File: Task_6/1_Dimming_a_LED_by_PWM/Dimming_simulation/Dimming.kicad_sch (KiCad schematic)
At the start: 6 parts, among them Q1 BC817

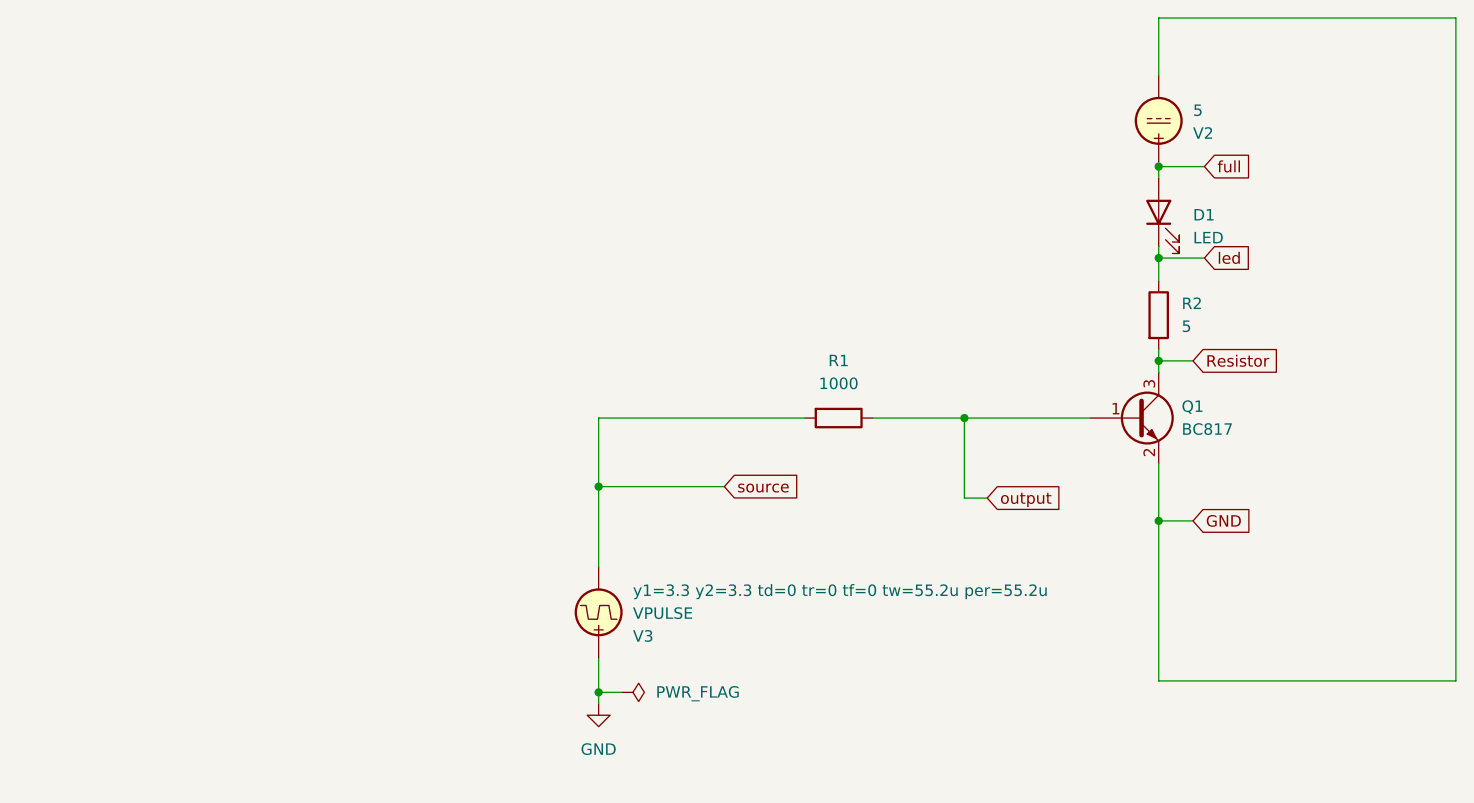
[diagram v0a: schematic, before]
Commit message: add simulation and measurement of current through LED
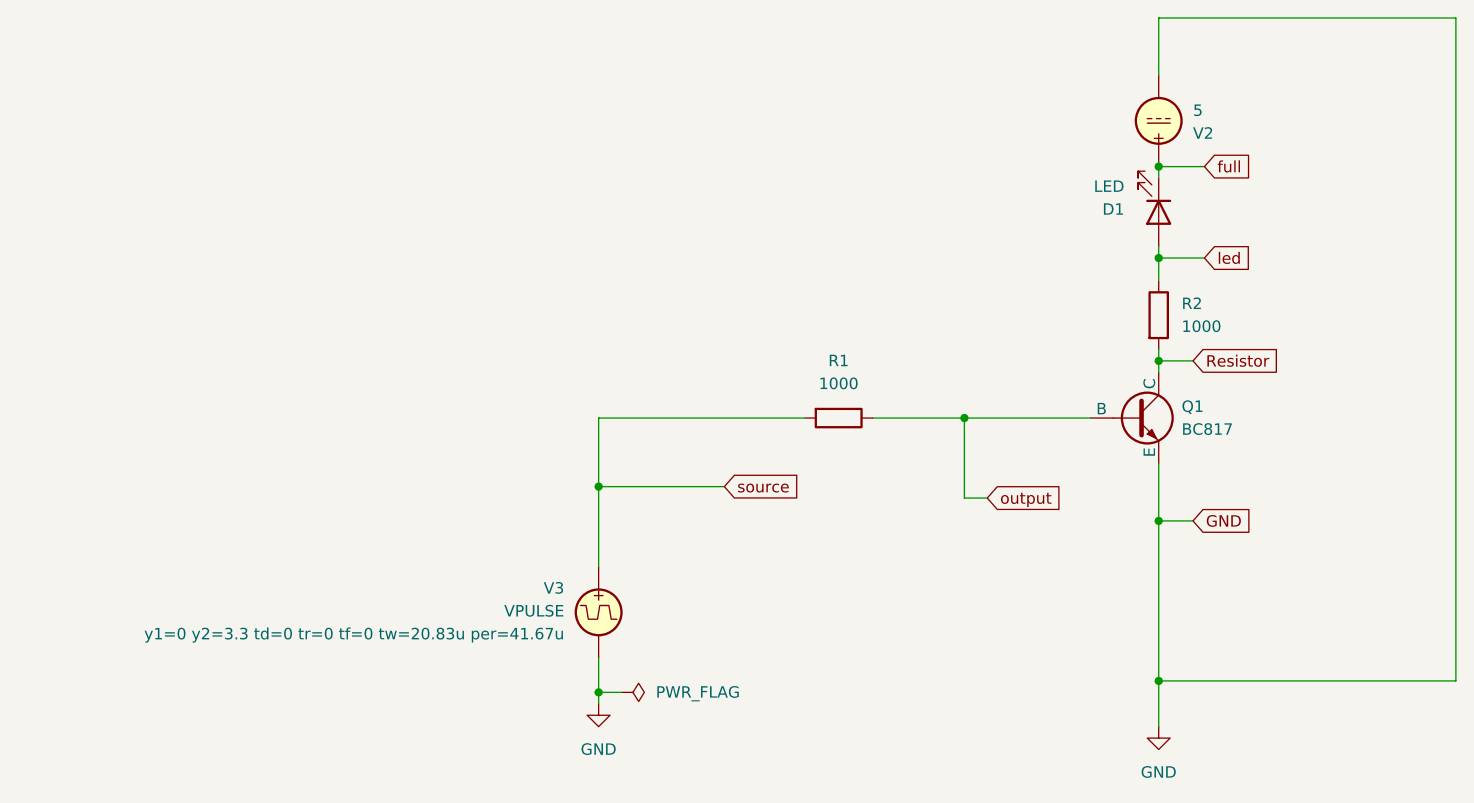
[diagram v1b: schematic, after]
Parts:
- removed Q1: BC817, Package_TO_SOT_SMD:SOT-23, symbol Transistor_BJT:BC817
- added Q1: BC817, symbol Simulation_SPICE:NPN
- R2: value 5 -> 1000
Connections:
- net GND: now also V3.2, Q1.3 (E); no longer V3.1
- net Resistor: now also Q1.1 (C)
- net full: now also D1.1 (K); no longer D1.2 (A)
- net led: now also D1.2 (A); no longer D1.1 (K)
- net output: now also Q1.2 (B)
- net source: now also V3.1; no longer V3.2
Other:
- moved on the sheet: D1
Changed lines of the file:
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@@
+	)
+	(junction
+		(at 146.05 113.03)
+		(diameter 0)
+		(color 0 0 0 0)
 	)
 	(junction
@@
 		(pts
 			(xy 149.86 77.47) (xy 146.05 77.47)
+		)
+		(stroke
+			(width 0)
+			(type default)
+		)
+	)
+	(wire
+		(pts
+			(xy 146.05 113.03) (xy 146.05 118.11)
 		)
 		(stroke
@@
 	(symbol
 		(lib_id "Device:LED")
-		(at 146.05 60.96 90)
+		(at 146.05 60.96 270)
 		(unit 1)
 		(exclude_from_sim no)
@@
 		(dnp no)
 		(property "Reference" "D1"
-			(at 149.86 61.2774 90)
+			(at 142.24 60.6426 90)
 			(effects
 				(font
@@
 		)
 		(property "Value" "LED"
-			(at 149.86 63.8174 90)
+			(at 142.24 58.1026 90)
 			(effects
 				(font
@@
 		(lib_id "Simulation_SPICE:VPULSE")
 		(at 83.82 105.41 0)
-		(mirror x)
+		(mirror y)
 		(unit 1)
 		(exclude_from_sim no)
@@
 		(dnp no)
 		(property "Reference" "V3"
-			(at 87.63 108.0799 0)
+			(at 80.01 102.7401 0)
 			(effects
 				(font
@@
 		)
 		(property "Value" "VPULSE"
-			(at 87.63 105.5399 0)
+			(at 80.01 105.2801 0)
 			(effects
 				(font
@@
 			)
 		)
-		(property "Sim.Params" "y1=3.3 y2=3.3 td=0 tr=0 tf=0 tw=55.2u per=55.2u"
-			(at 87.63 102.9999 0)
+		(property "Sim.Params" "y1=0 y2=3.3 td=0 tr=0 tf=0 tw=20.83u per=41.67u"
+			(at 80.01 107.8201 0)
 			(effects
 				(font
@@
 			)
 		)
-		(property "Value" "5"
+		(property "Value" "1000"
 			(at 148.59 73.6599 0)
 			(effects
@@
 	)
 	(symbol
-		(lib_id "Transistor_BJT:BC817")
+		(lib_id "Simulation_SPICE:NPN")
 		(at 143.51 83.82 0)
 		(unit 1)
@@
 		(on_board yes)
 		(dnp no)
+		(fields_autoplaced yes)
 		(property "Reference" "Q1"
 			(at 148.59 82.5499 0)
@@
 			)
 		)
-		(property "Footprint" "Package_TO_SOT_SMD:SOT-23"
-			(at 148.59 85.725 0)
-			(effects
-				(font
-					(size 1.27 1.27)
-					(italic yes)
-				)
-				(justify left)
-				(hide yes)
-			)
-		)
-		(property "Datasheet" "https://www.onsemi.com/pub/Collateral/BC818-D.pdf"
+		(property "Footprint" ""
+			(at 207.01 83.82 0)
+			(effects
+				(font
+					(size 1.27 1.27)
+				)
+				(hide yes)
+			)
+		)
+		(property "Datasheet" "https://ngspice.sourceforge.io/docs/ngspice-html-manual/manual.xhtml#cha_BJTs"
+			(at 207.01 83.82 0)
+			(effects
+				(font
+					(size 1.27 1.27)
+				)
+				(hide yes)
+			)
+		)
+		(property "Description" "Bipolar transistor symbol for simulation only, substrate tied to the emitter"
 			(at 143.51 83.82 0)
 			(effects
@@
 					(size 1.27 1.27)
 				)
-				(justify left)
-				(hide yes)
-			)
-		)
-		(property "Description" "0.8A Ic, 45V Vce, NPN Transistor, SOT-23"
+				(hide yes)
+			)
+		)
+		(property "Sim.Device" "SUBCKT"
+			(at 143.51 83.82 0)
+			(effects
+				(font
+					(size 1.27 1.27)
+				)
+				(hide yes)
+			)
+		)
+		(property "Sim.Pins" "1=1 2=2 3=3"
 			(at 143.51 83.82 0)
 			(effects
@@
 			)
 		)
-		(property "Sim.Device" "SUBCKT"
-			(at 143.51 83.82 0)
-			(effects
-				(font
-					(size 1.27 1.27)
-				)
-				(hide yes)
-			)
-		)
-		(property "Sim.Pins" "1=1 2=2 3=3"
-			(at 143.51 83.82 0)
-			(effects
-				(font
-					(size 1.27 1.27)
-				)
-				(hide yes)
-			)
+		(pin "2"
+		)
+		(pin "3"
 		)
 		(pin "1"
-		)
-		(pin "3"
-		)
-		(pin "2"
 		)
 		(instances
@@
 					(unit 1)
 				)
+			)
+		)
+	)
+	(symbol
+		(lib_id "power:GND")
+		(at 146.05 118.11 0)
+		(unit 1)
+		(exclude_from_sim no)
+		(in_bom yes)
+		(on_board yes)
+		(dnp no)
+		(fields_autoplaced yes)
+		(property "Reference" "#PWR02"
+			(at 146.05 124.46 0)
+			(effects
+				(font
+					(size 1.27 1.27)
+				)
+				(hide yes)
+			)
+		)
+		(property "Value" "GND"
+			(at 146.05 123.19 0)
+			(effects
+				(font
+					(size 1.27 1.27)
+				)
+			)
+		)
+		(property "Footprint" ""
+			(at 146.05 118.11 0)
+			(effects
+				(font
+					(size 1.27 1.27)
+				)
+				(hide yes)
+			)
+		)
+		(property "Datasheet" ""
+			(at 146.05 118.11 0)
+			(effects
+				(font
+					(size 1.27 1.27)
+				)
+				(hide yes)
+			)
+		)
+		(property "Description" "Power symbol creates a global label with name \"GND\" , ground"
+			(at 146.05 118.11 0)
+			(effects
+				(font
+					(size 1.27 1.27)
+				)
+				(hide yes)
+			)
+		)
+		(pin "1"
+		)
+		(instances
+			(project ""
+				(path "/b0c10853-3f7b-40c1-b1d0-8a6433951273"
+					(reference "#PWR02")
+					(unit 1)
+				)
